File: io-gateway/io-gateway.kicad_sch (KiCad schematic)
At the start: 46 parts, among them IC1 MAX17673AATI+

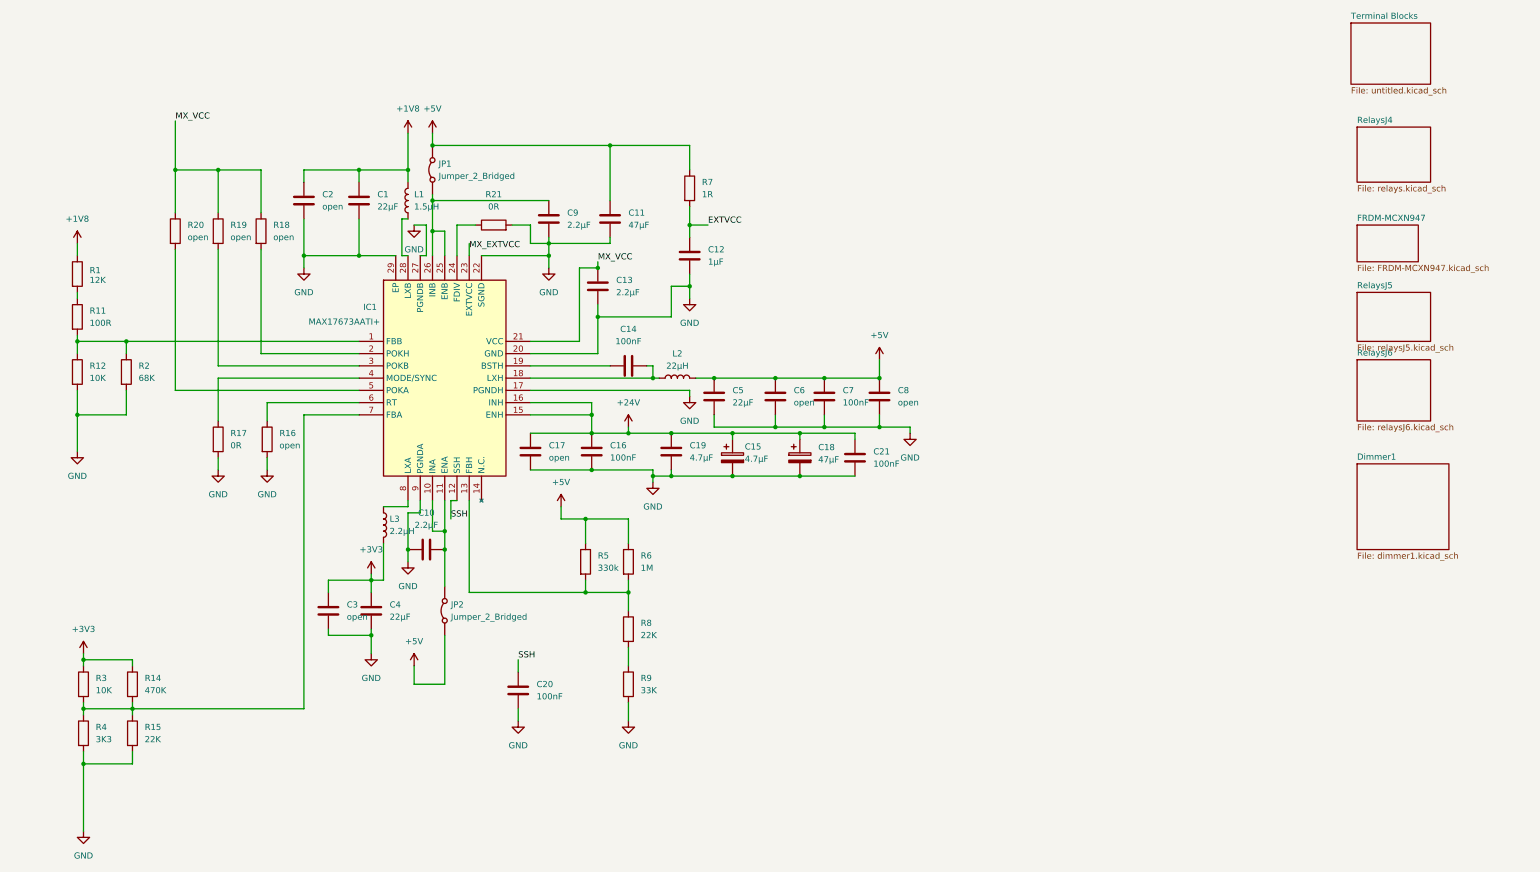
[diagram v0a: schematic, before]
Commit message: add voltage regulator
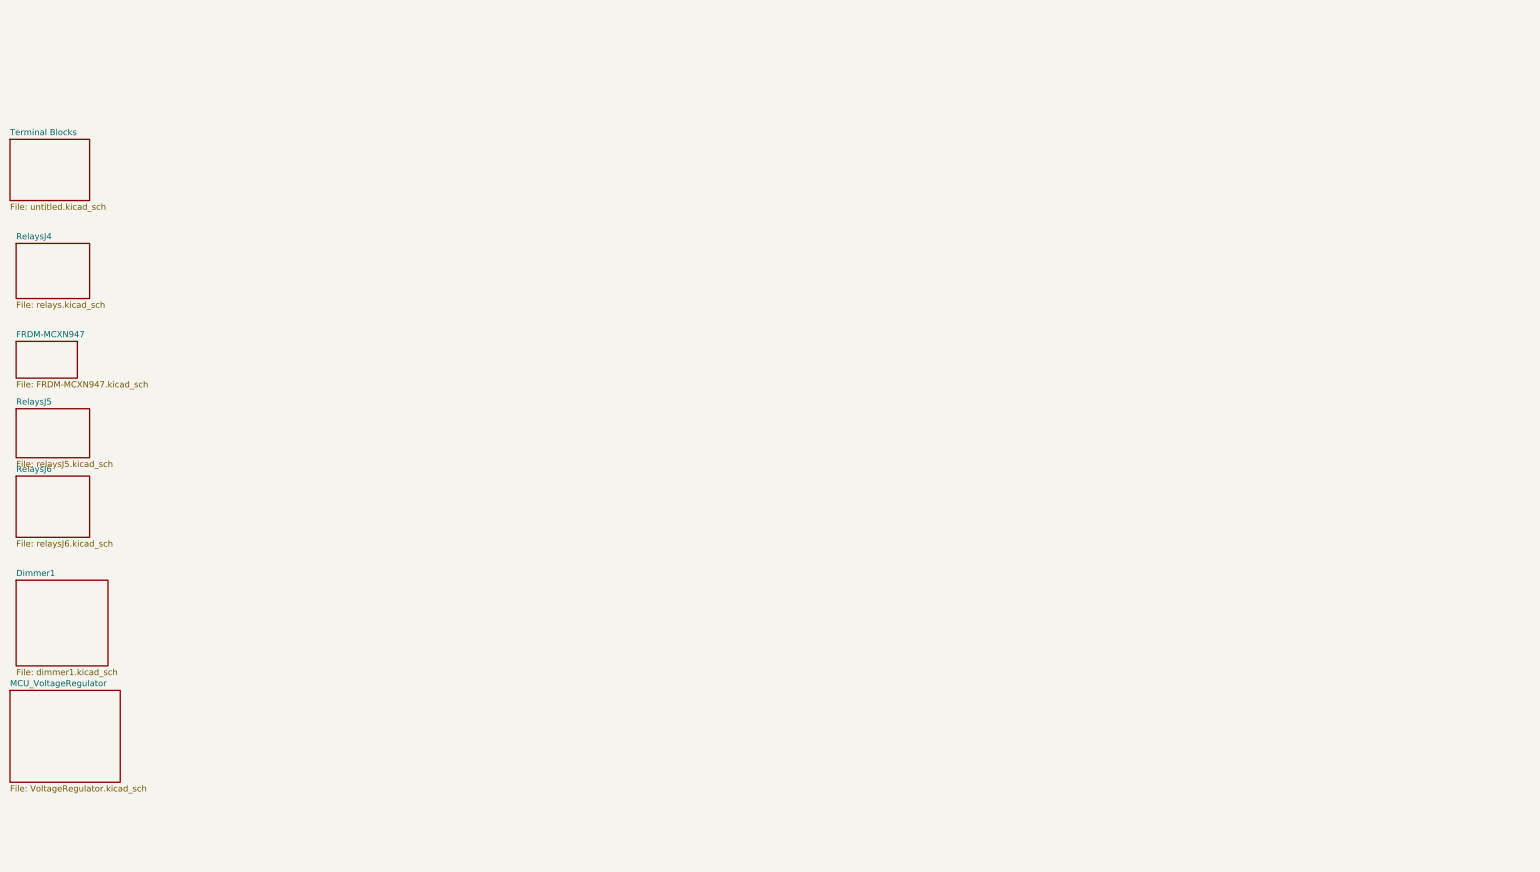
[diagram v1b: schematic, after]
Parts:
- removed C1, C4, C5: 22µF, Capacitor_SMD:C_0603_1608Metric, symbol Device:C
- removed C10, C13, C9: 2.2µF, Capacitor_SMD:C_0603_1608Metric, symbol Device:C
- removed C11: 47µF, Capacitor_SMD:C_0603_1608Metric, symbol Device:C
- removed C12: 1µF, Capacitor_SMD:C_0603_1608Metric, symbol Device:C
- removed C14, C16, C20, C21, C7: 100nF, Capacitor_SMD:C_0603_1608Metric, symbol Device:C
- removed C15: 4.7µF, Capacitor_SMD:CP_Elec_4x5.4, symbol Device:C_Polarized
- removed C17, C2, C3, C6, C8: open, Capacitor_SMD:C_0603_1608Metric, symbol Device:C
- removed C18: 47µF, Capacitor_SMD:CP_Elec_6.3x5.4, symbol Device:C_Polarized
- removed C19: 4.7µF, Capacitor_SMD:C_0603_1608Metric, symbol Device:C
- removed IC1: MAX17673AATI+, Package_DFN_QFN:QFN50P500X500X80-29N, symbol MAX17673AATI+:MAX17673AATI+
- removed JP1, JP2: Jumper_2_Bridged, TestPoint:TestPoint_2Pads_Pitch2.54mm_Drill0.8mm, symbol Jumper:Jumper_2_Bridged
- removed L1: 1.5µH, Inductor_SMD:L_1210_3225Metric, symbol Device:L
- removed L2: 22µH, Inductor_SMD:L_1008_2520Metric, symbol Device:L
- removed L3: 2.2µH, Inductor_SMD:L_1210_3225Metric, symbol Device:L
- removed R1: 12K, Resistor_SMD:R_0201_0603Metric, symbol Device:R
- removed R11: 100R, Resistor_SMD:R_0201_0603Metric, symbol Device:R
- removed R12, R3: 10K, Resistor_SMD:R_0201_0603Metric, symbol Device:R
- removed R14: 470K, Resistor_SMD:R_0201_0603Metric, symbol Device:R
- removed R15, R8: 22K, Resistor_SMD:R_0201_0603Metric, symbol Device:R
- removed R16, R18, R19, R20: open, Resistor_SMD:R_0201_0603Metric, symbol Device:R
- removed R17, R21: 0R, Resistor_SMD:R_0201_0603Metric, symbol Device:R
- removed R2: 68K, Resistor_SMD:R_0201_0603Metric, symbol Device:R
- removed R4: 3K3, Resistor_SMD:R_0201_0603Metric, symbol Device:R
- removed R5: 330k, Resistor_SMD:R_0201_0603Metric, symbol Device:R
- removed R6: 1M, Resistor_SMD:R_0201_0603Metric, symbol Device:R
- removed R7: 1R, Resistor_SMD:R_0201_0603Metric, symbol Device:R
- removed R9: 33K, Resistor_SMD:R_0201_0603Metric, symbol Device:R
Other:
- added sheet MCU_VoltageRegulator (VoltageRegulator.kicad_sch)

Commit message: temp
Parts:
- added D1: SMBJ28A, TVS_Diodes:DIOM5436X244N, symbol SMBJ28A:SMBJ28A
- added F1: Fuse, Fuse:Fuseholder_Cylinder-5x20mm_Wuerth_696103101002-SMD_Horizontal_Open, symbol Device:Fuse
- added J1, J2, J3: 1752201, TerminalBlock_Phoenix:1752201, symbol 1752201:1752201
- added J4, J5, J6: Screw_Terminal_01x09, TerminalBlock_TE-Connectivity:TerminalBlock_TE_282836-9_1x09_P5mm_Horizontal, symbol Connector:Screw_Terminal_01x09
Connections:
- new net +24V: D1.1 (K), F1.2
- new net ANALOG_IN_1: J1.5
- new net ANALOG_IN_2: J1.6
- new net DIM10_VLED_GND: J3.12
- new net DIM10_VLED_VCC: J3.11
- new net DIM1_VLED_GND: J1.10
- new net DIM1_VLED_VCC: J1.9
- new net DIM2_VLED_GND: J1.12
- new net DIM2_VLED_VCC: J1.11
- new net DIM3_VLED_GND: J2.4
- new net DIM3_VLED_VCC: J2.3
- new net DIM4_VLED_GND: J2.6
- new net DIM4_VLED_VCC: J2.5
- new net DIM5_VLED_GND: J2.10
- new net DIM5_VLED_VCC: J2.9
- new net DIM6_VLED_GND: J2.12
- new net DIM6_VLED_VCC: J2.11
- new net DIM7_VLED_GND: J3.4
- new net DIM7_VLED_VCC: J3.3
- new net DIM8_VLED_GND: J3.6
- new net DIM8_VLED_VCC: J3.5
- new net DIM9_VLED_GND: J3.10
- new net DIM9_VLED_VCC: J3.9
- new net Dimmer1/GND_DIM: J1.8
- new net Dimmer1/VIN_DIM: J1.7
- new net GND: D1.2 (A), J1.2
- new net GND_DIM3: J2.2, J3.2
- new net GND_DIM5: J2.8, J3.8
- new net RS485_A: J1.3
- new net RS485_B: J1.4
- new net Relay4/VAC_IN: J5.1 (Pin_1)
- new net Relay4/VAC_OUT: J5.2 (Pin_2)
- new net Relay5/VAC_IN: J5.4 (Pin_4)
- new net Relay5/VAC_OUT: J5.5 (Pin_5)
- new net Relay6/VAC_IN: J5.7 (Pin_7)
- new net Relay6/VAC_OUT: J5.8 (Pin_8)
- new net Relay7/VAC_IN: J6.1 (Pin_1)
- new net Relay7/VAC_OUT: J6.2 (Pin_2)
- new net Relay8/VAC_IN: J6.4 (Pin_4)
- new net Relay8/VAC_OUT: J6.5 (Pin_5)
- new net Relay9/VAC_IN: J6.7 (Pin_7)
- new net Relay9/VAC_OUT: J6.8 (Pin_8)
- new net VAC_IN_1: J4.1 (Pin_1)
- new net VAC_IN_2: J4.4 (Pin_4)
- new net VAC_IN_3: J4.7 (Pin_7)
- new net VAC_OUT_1.1: J4.2 (Pin_2)
- new net VAC_OUT_2.1: J4.5 (Pin_5)
- new net VAC_OUT_3.1: J4.8 (Pin_8)
- new net VDC_CTRL: F1.1, J1.1
- new net VIN_DIM3: J2.1, J3.1
- new net VIN_DIM5: J2.7, J3.7
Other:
- sheet RelaysJ4 renamed Relay1
- sheet RelaysJ6 renamed RS485
- added sheet Relay2 (relays.kicad_sch)
- added sheet Relay3 (relays.kicad_sch)
- added sheet Relay4 (relays.kicad_sch)
- added sheet Relay5 (relays.kicad_sch)
- added sheet Relay6 (relays.kicad_sch)
- added sheet Relay7 (relays.kicad_sch)
- added sheet Relay8 (relays.kicad_sch)
- added sheet Relay9 (relays.kicad_sch)
- sheet Dimmer1 ports: added DIM_VLED+_A, DIM_VLED+_B, DIM_VLED-_A, DIM_VLED-_B, GND_DIM, INH_DIMA, INH_DIMB, PWM_DIMA, PWM_DIMB, VIN_DIM; removed none
- sheet Relay1 ports: added SW_IN, VAC_IN, VAC_OUT; removed none
